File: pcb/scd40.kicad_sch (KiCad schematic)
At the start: 7 parts, among them J7 I2C Board, J8 I2C Sensor, U4 SCD40-D-R2

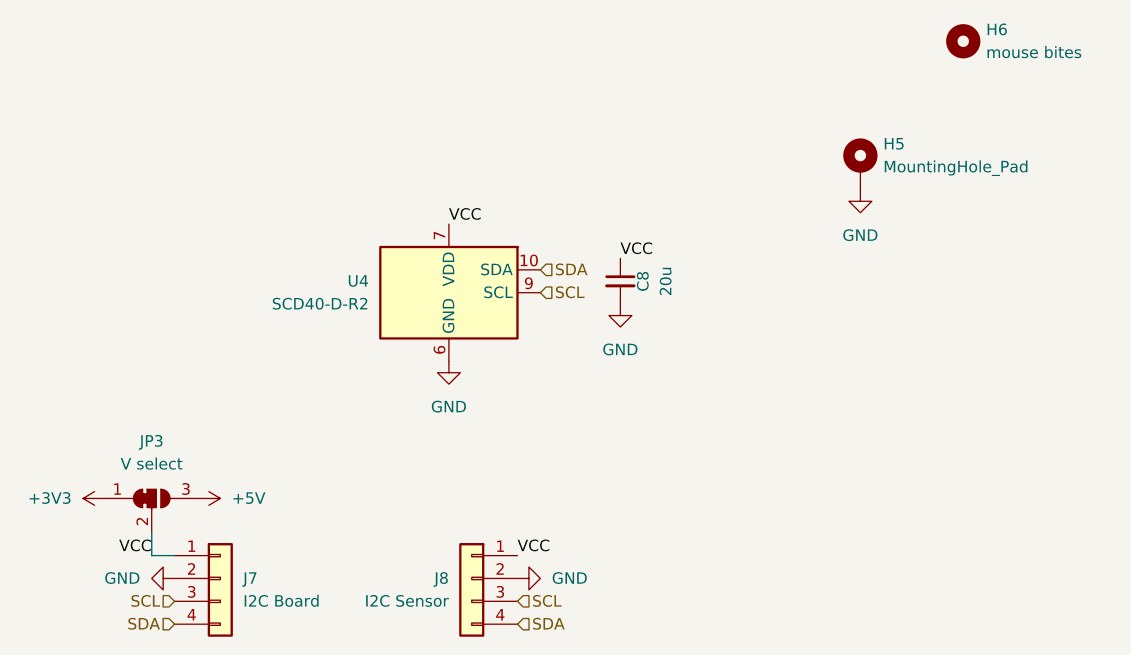
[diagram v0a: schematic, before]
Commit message: Rename pcb, add sensors and fix some issues
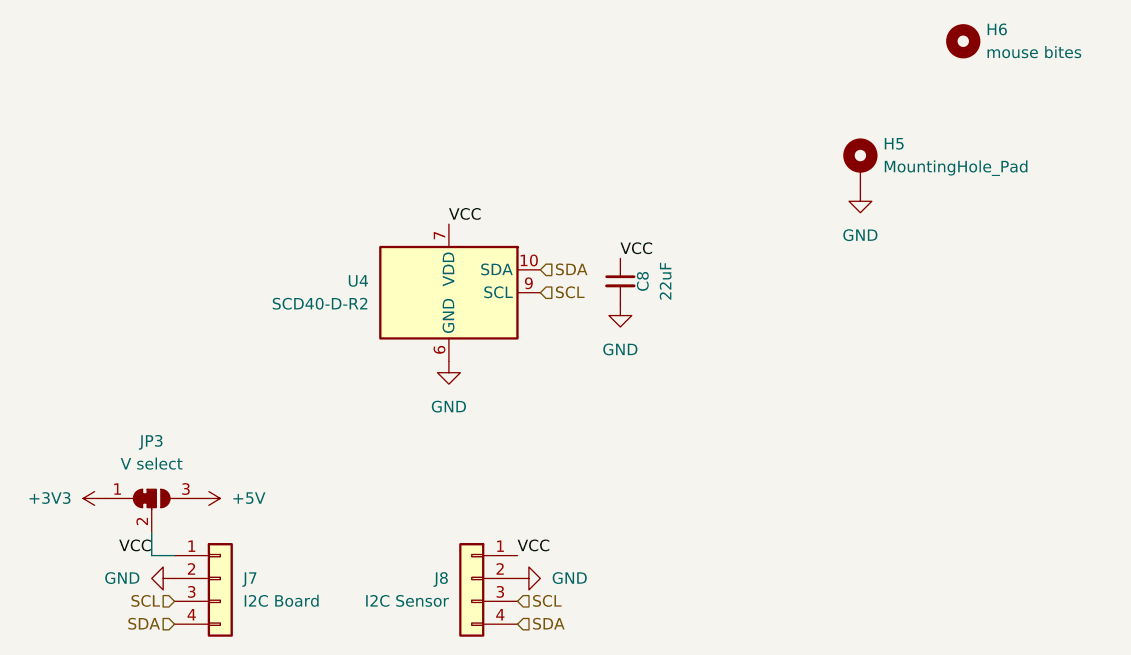
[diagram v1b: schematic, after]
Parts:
- C8: value 20u -> 22uF
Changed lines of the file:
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@@
 			)
 		)
-		(property "Value" "20u"
+		(property "Value" "22uF"
 			(at 93.98 71.12 90)
 			(effects
